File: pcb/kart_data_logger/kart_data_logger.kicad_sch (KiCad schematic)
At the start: 20 parts, among them J1 GPS, J2 I2S AMP, J3 Battery, Q1 BC327, Q2 2N3904, Q3 2N3904, SW1 ON/OFF, U2 XIAO-ESP32-S3-SMD

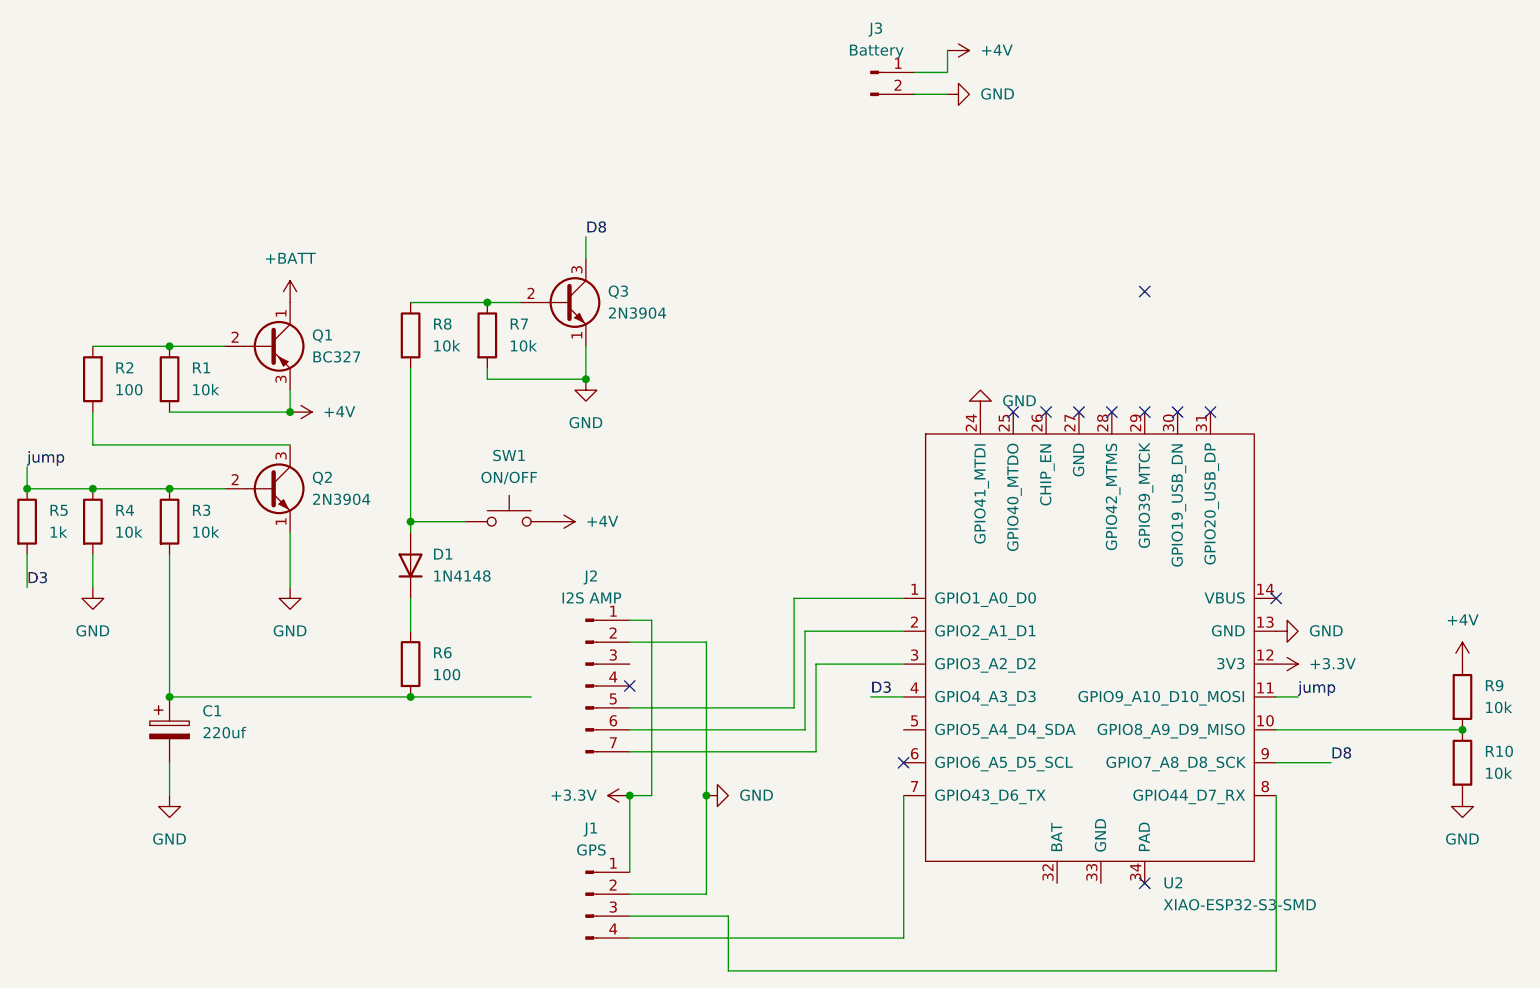
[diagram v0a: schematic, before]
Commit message: updated KiCad project files; updated platformio.ini to change upload port and include MPU6050 library for IMU support; modified main_display.cpp to integrate IMU data handling and adjust telemetry based on GPS provider; refactored main_logger.cpp to streamline IMU data retrieval and telemetry message construction; improved initialization sequence for IMU and display components in setup functions;
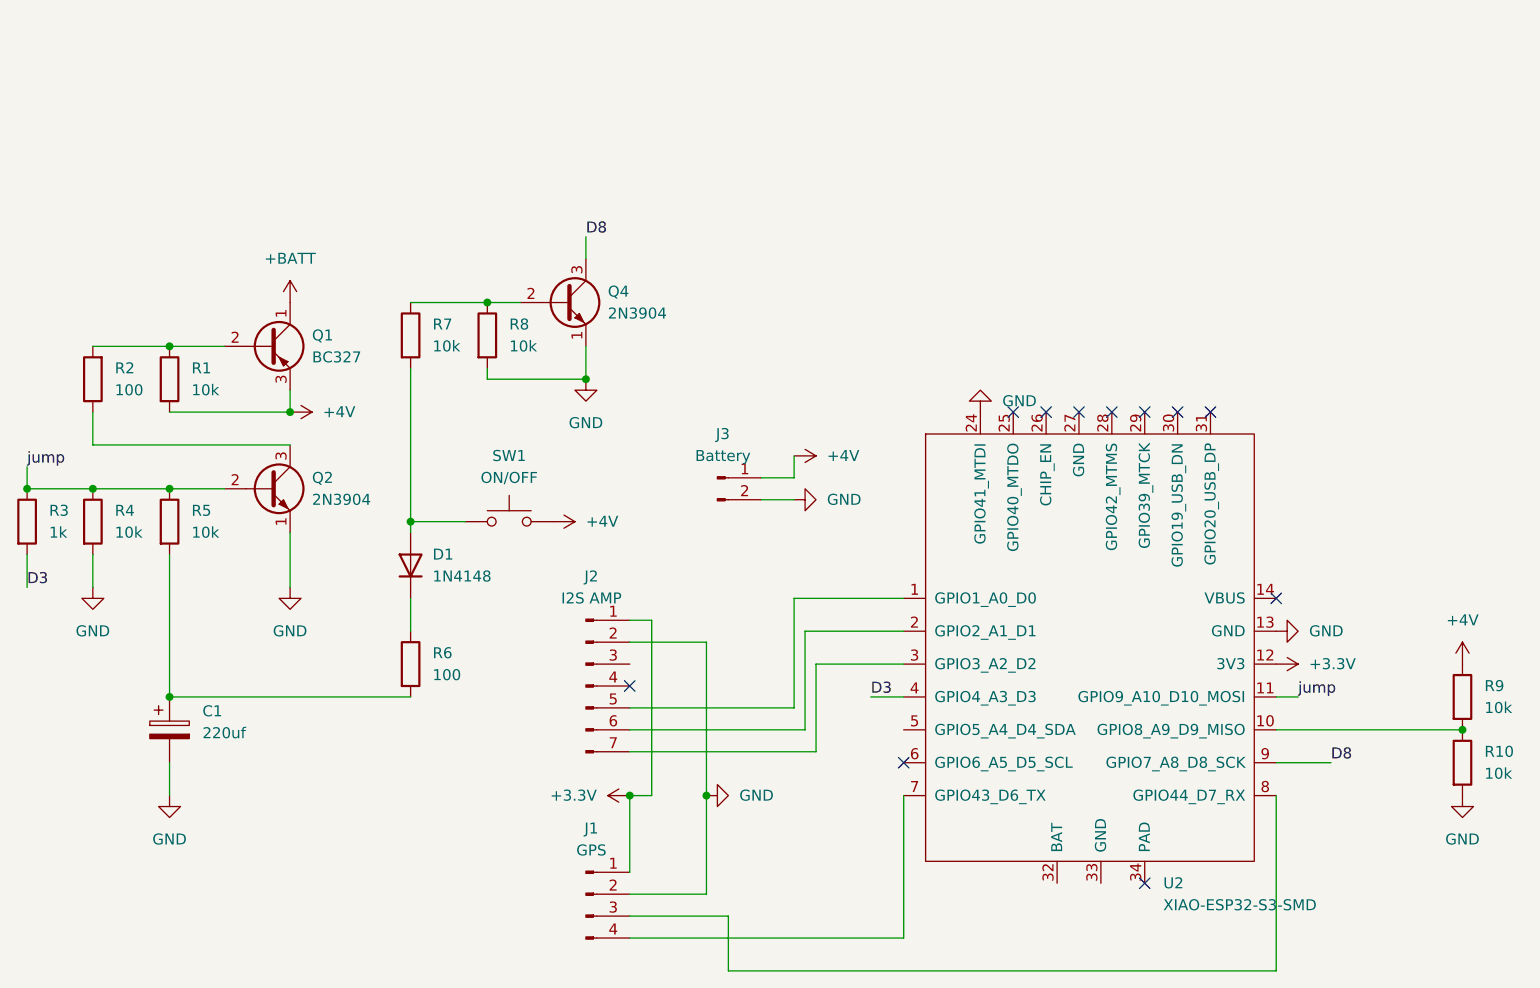
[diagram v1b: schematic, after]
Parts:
- C1: footprint Capacitor_THT:CP_Radial_D12.5mm_P5.00mm -> Capacitor_THT:CP_Radial_D6.3mm_P2.50mm
- SW1: footprint (none) -> Connector_PinHeader_2.54mm:PinHeader_1x02_P2.54mm_Vertical
- renumbered Q3 to Q4, R5 to R3, R3 to R5, R8 to R7, R7 to R8
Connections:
- no-connect marks 12 -> 11
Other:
- moved on the sheet: J3
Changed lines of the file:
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@@
 	)
 	(junction
-		(at 20.32 77.47)
-		(diameter 0)
-		(color 0 0 0 0)
-	)
-	(junction
 		(at 85.09 64.77)
 		(diameter 0)
@@
 	)
 	(junction
-		(at 36.83 77.47)
+		(at 20.32 77.47)
 		(diameter 0)
 		(color 0 0 0 0)
 	)
 	(junction
-		(at 64.77 101.6)
+		(at 36.83 77.47)
 		(diameter 0)
 		(color 0 0 0 0)
@@
 	)
 	(no_connect
-		(at 149.86 54.61)
-	)
-	(no_connect
 		(at 121.92 109.22)
 	)
@@
 	(wire
 		(pts
-			(xy 123.19 29.21) (xy 127 29.21)
+			(xy 105.41 76.2) (xy 109.22 76.2)
 		)
 		(stroke
@@
 	(wire
 		(pts
-			(xy 20.32 74.93) (xy 20.32 77.47)
+			(xy 92.71 113.03) (xy 90.17 113.03)
 		)
 		(stroke
@@
 	(wire
 		(pts
-			(xy 92.71 113.03) (xy 90.17 113.03)
+			(xy 105.41 78.74) (xy 109.22 78.74)
 		)
 		(stroke
@@
 	(wire
 		(pts
-			(xy 123.19 31.75) (xy 127 31.75)
+			(xy 109.22 76.2) (xy 109.22 73.66)
 		)
 		(stroke
@@
 	(wire
 		(pts
-			(xy 127 29.21) (xy 127 26.67)
+			(xy 110.49 105.41) (xy 110.49 93.98)
 		)
 		(stroke
@@
 	(wire
 		(pts
-			(xy 110.49 105.41) (xy 110.49 93.98)
+			(xy 36.83 109.22) (xy 36.83 113.03)
 		)
 		(stroke
@@
 	(wire
 		(pts
-			(xy 36.83 109.22) (xy 36.83 113.03)
+			(xy 109.22 90.17) (xy 121.92 90.17)
 		)
 		(stroke
@@
 	(wire
 		(pts
-			(xy 109.22 90.17) (xy 121.92 90.17)
+			(xy 99.06 95.25) (xy 99.06 113.03)
 		)
 		(stroke
@@
 	(wire
 		(pts
-			(xy 99.06 95.25) (xy 99.06 113.03)
+			(xy 50.8 68.58) (xy 50.8 66.04)
 		)
 		(stroke
@@
 	(wire
 		(pts
-			(xy 50.8 68.58) (xy 50.8 66.04)
+			(xy 20.32 74.93) (xy 20.32 77.47)
 		)
 		(stroke
@@
 	(wire
 		(pts
-			(xy 64.77 101.6) (xy 78.74 101.6)
-		)
-		(stroke
-			(width 0)
-			(type default)
-		)
-	)
-	(wire
-		(pts
 			(xy 73.66 64.77) (xy 85.09 64.77)
 		)
@@
 		(dnp no)
 		(fields_autoplaced yes)
-		(property "Reference" "R3"
+		(property "Reference" "R5"
 			(at 39.37 80.0099 0)
 			(show_name no)
@@
 			(project "kart_data_logger"
 				(path "/301bd5d2-ee50-4328-bd4b-0bdabdaa4add"
-					(reference "R3")
+					(reference "R5")
 					(unit 1)
 				)
@@
 			)
 		)
-		(property "Footprint" ""
+		(property "Footprint" "Connector_PinHeader_2.54mm:PinHeader_1x02_P2.54mm_Vertical"
 			(at 76.2 76.2 0)
 			(hide yes)
@@
 		(dnp no)
 		(fields_autoplaced yes)
-		(property "Reference" "Q3"
+		(property "Reference" "Q4"
 			(at 87.63 54.6099 0)
 			(show_name no)
@@
 			(project "kart_data_logger"
 				(path "/301bd5d2-ee50-4328-bd4b-0bdabdaa4add"
-					(reference "Q3")
+					(reference "Q4")
 					(unit 1)
 				)
@@
 		(dnp no)
 		(fields_autoplaced yes)
-		(property "Reference" "R5"
+		(property "Reference" "R3"
 			(at 22.86 80.0099 0)
 			(show_name no)
@@
 			(project "kart_data_logger"
 				(path "/301bd5d2-ee50-4328-bd4b-0bdabdaa4add"
-					(reference "R5")
+					(reference "R3")
 					(unit 1)
 				)
@@
 			)
 		)
-		(property "Footprint" "Capacitor_THT:CP_Radial_D12.5mm_P5.00mm"
+		(property "Footprint" "Capacitor_THT:CP_Radial_D6.3mm_P2.50mm"
 			(at 37.7952 109.22 0)
 			(hide yes)
@@
 		(in_pos_files yes)
 		(dnp no)
-		(property "Reference" "R8"
+		(property "Reference" "R7"
 			(at 67.31 58.4199 0)
 			(show_name no)
@@
 			(project "kart_data_logger"
 				(path "/301bd5d2-ee50-4328-bd4b-0bdabdaa4add"
-					(reference "R8")
+					(reference "R7")
 					(unit 1)
 				)
@@
 		(dnp no)
 		(fields_autoplaced yes)
-		(property "Reference" "R7"
+		(property "Reference" "R8"
 			(at 76.2 58.4199 0)
 			(show_name no)
@@
 			(project "kart_data_logger"
 				(path "/301bd5d2-ee50-4328-bd4b-0bdabdaa4add"
-					(reference "R7")
+					(reference "R8")
 					(unit 1)
 				)
@@
 	(symbol
 		(lib_id "Connector:Conn_01x02_Pin")
-		(at 118.11 29.21 0)
+		(at 100.33 76.2 0)
 		(unit 1)
 		(body_style 1)
@@
 		(fields_autoplaced yes)
 		(property "Reference" "J3"
-			(at 118.745 24.13 0)
+			(at 100.965 71.12 0)
 			(show_name no)
 			(do_not_autoplace no)
@@
 		)
 		(property "Value" "Battery"
-			(at 118.745 26.67 0)
+			(at 100.965 73.66 0)
 			(show_name no)
 			(do_not_autoplace no)
@@
 		)
 		(property "Footprint" "Connector_PinHeader_2.54mm:PinHeader_1x02_P2.54mm_Vertical"
-			(at 118.11 29.21 0)
+			(at 100.33 76.2 0)
 			(hide yes)
 			(show_name no)
@@
 		)
 		(property "Datasheet" ""
-			(at 118.11 29.21 0)
+			(at 100.33 76.2 0)
 			(hide yes)
 			(show_name no)
@@
 		)
 		(property "Description" "Generic connector, single row, 01x02, script generated"
-			(at 118.11 29.21 0)
+			(at 100.33 76.2 0)
 			(hide yes)
 			(show_name no)
@@
 	(symbol
 		(lib_id "power:+4V")
-		(at 127 26.67 270)
+		(at 109.22 73.66 270)
 		(unit 1)
 		(body_style 1)
@@
 		(fields_autoplaced yes)
 		(property "Reference" "#PWR05"
-			(at 123.19 26.67 0)
+			(at 105.41 73.66 0)
 			(hide yes)
 			(show_name no)
@@
 		)
 		(property "Value" "+4V"
-			(at 130.81 26.6699 90)
+			(at 113.03 73.6599 90)
 			(show_name no)
 			(do_not_autoplace no)
@@
 		)
 		(property "Footprint" ""
-			(at 127 26.67 0)
+			(at 109.22 73.66 0)
 			(hide yes)
 			(show_name no)
@@
 		)
 		(property "Datasheet" ""
-			(at 127 26.67 0)
+			(at 109.22 73.66 0)
 			(hide yes)
 			(show_name no)
@@
 		)
 		(property "Description" "Power symbol creates a global label with name \"+4V\""
-			(at 127 26.67 0)
+			(at 109.22 73.66 0)
 			(hide yes)
 			(show_name no)
@@
 	(symbol
 		(lib_id "power:GND")
-		(at 127 31.75 90)
+		(at 109.22 78.74 90)
 		(unit 1)
 		(body_style 1)
@@
 		(fields_autoplaced yes)
 		(property "Reference" "#PWR02"
-			(at 133.35 31.75 0)
+			(at 115.57 78.74 0)
 			(hide yes)
 			(show_name no)
@@
 		)
 		(property "Value" "GND"
-			(at 130.81 31.7499 90)
+			(at 113.03 78.7399 90)
 			(show_name no)
 			(do_not_autoplace no)
@@
 		)
 		(property "Footprint" ""
-			(at 127 31.75 0)
+			(at 109.22 78.74 0)
 			(hide yes)
 			(show_name no)
@@
 		)
 		(property "Datasheet" ""
-			(at 127 31.75 0)
+			(at 109.22 78.74 0)
 			(hide yes)
 			(show_name no)
@@
 		)
 		(property "Description" "Power symbol creates a global label with name \"GND\" , ground"
-			(at 127 31.75 0)
+			(at 109.22 78.74 0)
 			(hide yes)
 			(show_name no)
